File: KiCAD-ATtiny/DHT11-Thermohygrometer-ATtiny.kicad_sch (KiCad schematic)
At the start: 15 parts, among them J1 ICSP, J2 DHT_Con, J3 1602_Con, J4 Batt_Con, J5 DHT_Con2, U1 ATtiny85V-10P, U2 DHT11, U3 LP2950-3.0_TO92

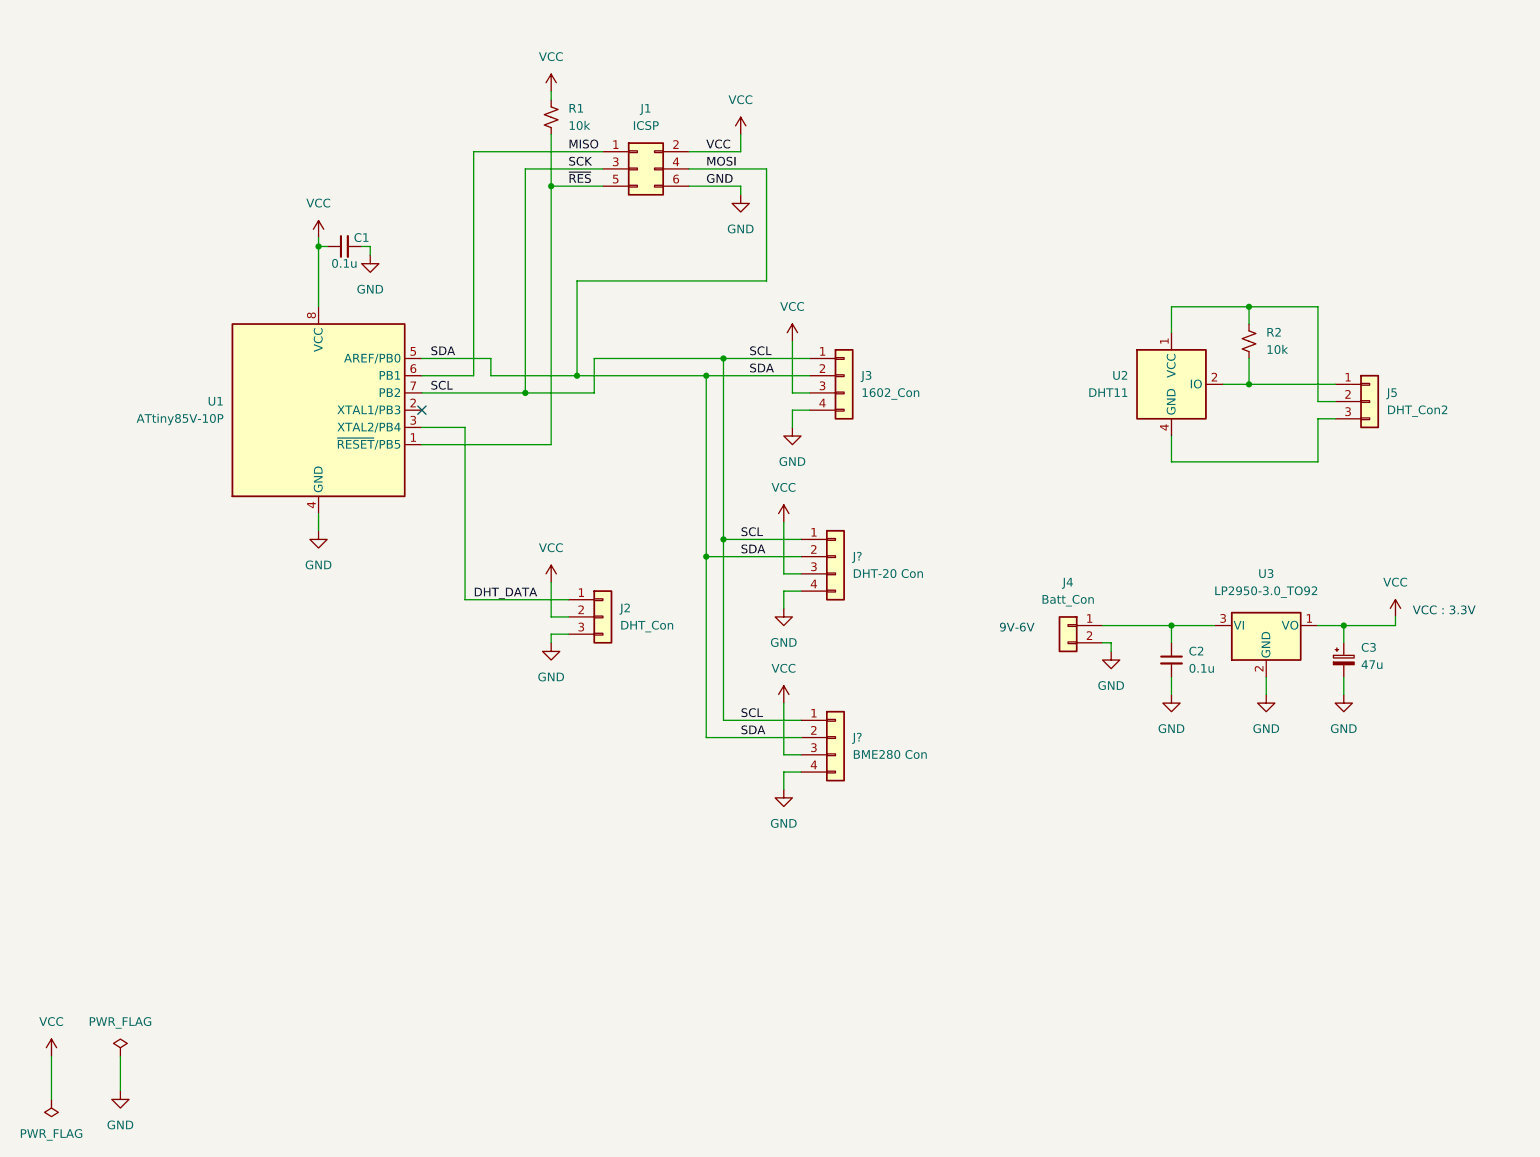
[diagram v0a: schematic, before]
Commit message: ATtiny回路図に プルアップ抵抗追加
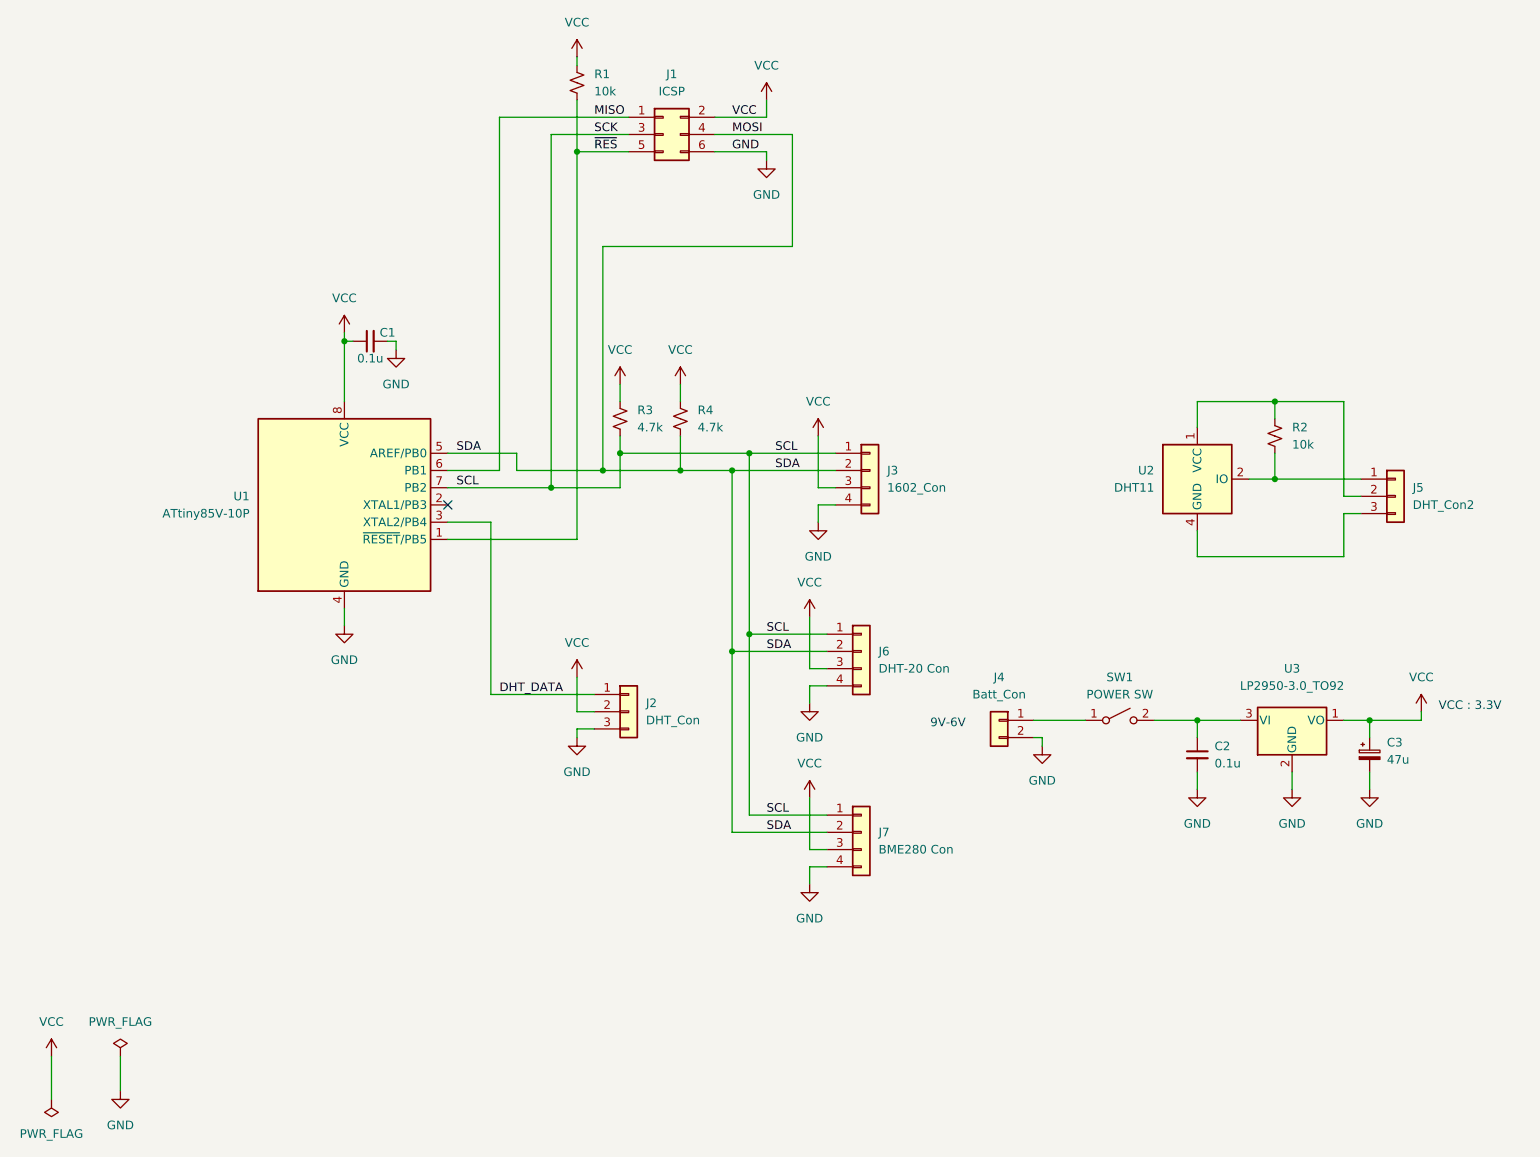
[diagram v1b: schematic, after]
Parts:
- added R3, R4: 4.7k, symbol Device:R_Small_US
- added SW1: POWER SW, symbol Switch:SW_SPST
- gave numbers to parts that had none: 2
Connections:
- net MOSI: now also R4.2
- net SCK: now also R3.2
- net VCC: now also R3.1, R4.1
- net at C2.1, U3.3 (VI): now also SW1.2 (B); no longer J4.1 (Pin_1)
- new net: J4.1 (Pin_1), SW1.1 (A)
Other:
- moved on the sheet: C1, C2, C3, J1, J2, J3, J4, J5, J6, J7, R1, R2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
